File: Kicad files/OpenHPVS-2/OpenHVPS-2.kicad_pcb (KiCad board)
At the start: 2 copper layers, 45.8 x 20.5 mm, 69 parts, among them J1 Conn_01x03_Male, J2 Conn_01x03_Male, Q1 FQT7N10, Q2 BC846A, Q3 MMDT3906, U1 MAX6008AEUR+T, U2 74HC14, U3 MAX4162, U4 CD14538BM

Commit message: Forgot the supply to the opamp - added. changed a capacitor value
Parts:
- C1: value 0.1uF -> 150pF
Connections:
- C2 pad 1: Net-(C2-Pad1) -> Net-(U3-Pad5)
- R5 pad 1: Net-(C2-Pad1) -> Net-(U3-Pad5)
- U2 pad 14: Net-(C2-Pad1) -> Net-(U3-Pad5)
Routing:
- net Net-(U3-Pad5): track 0.00 -> 8.95 mm
- net Net-(C2-Pad1): track 8.95 -> 0.00 mm

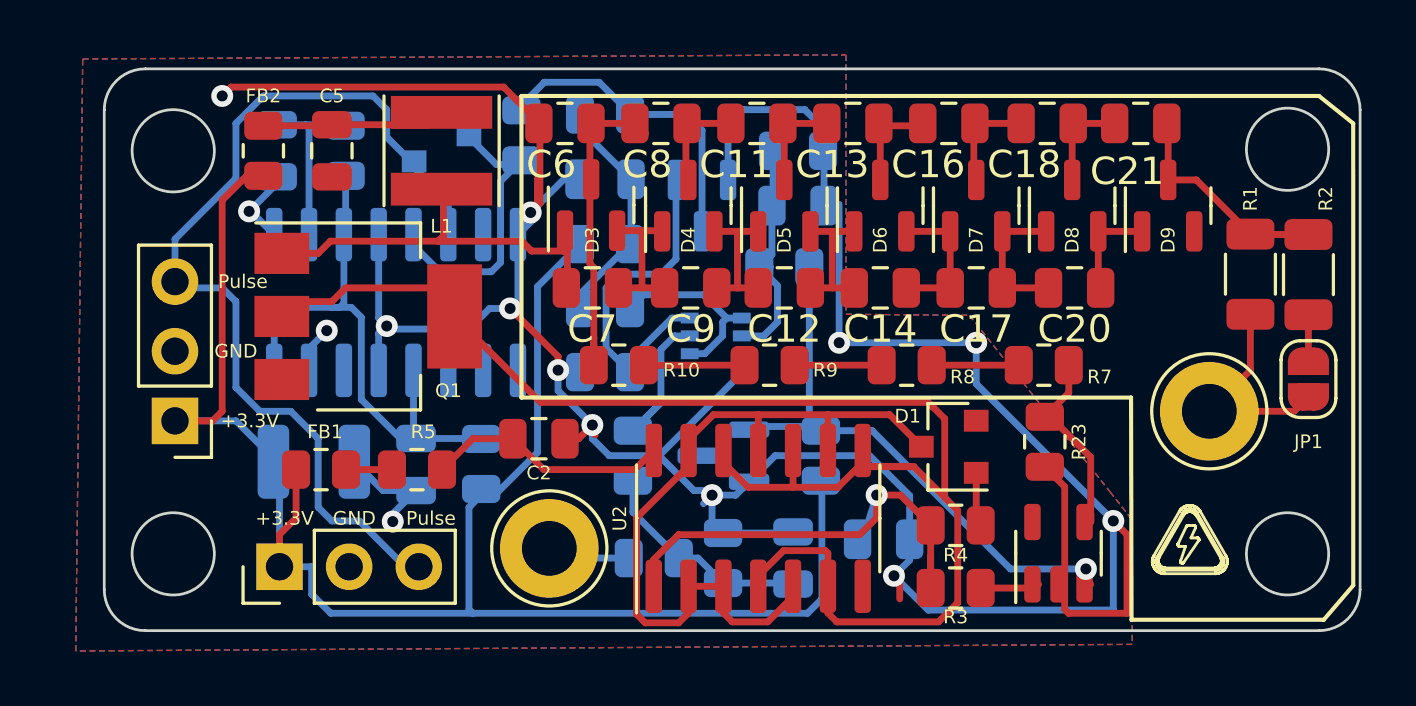
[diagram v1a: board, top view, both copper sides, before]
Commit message: Added space at  bottom and routed  track +graphic.
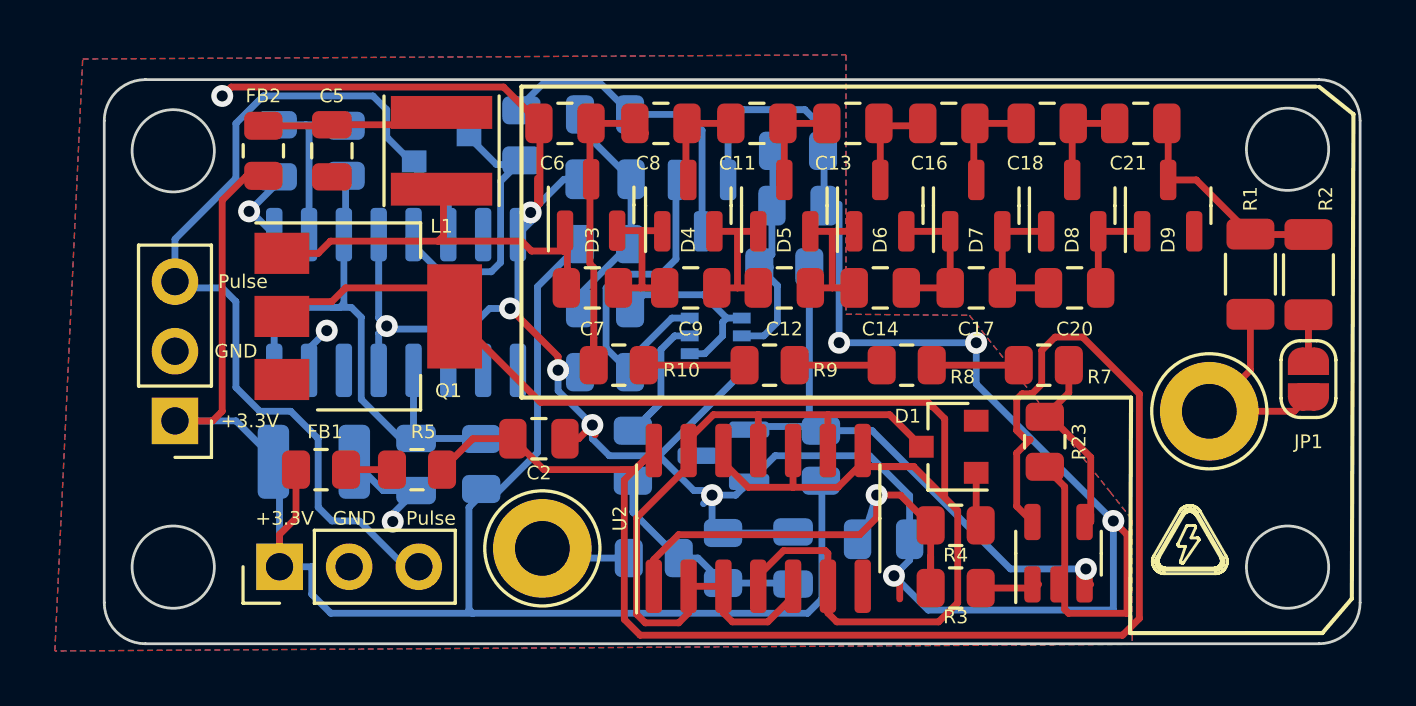
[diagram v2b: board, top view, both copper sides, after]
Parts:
- moved H1 0.25 mm to (138.2, 74.5)
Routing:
- net Net-(U3-Pad5): track 8.95 -> 55.2 mm
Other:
- board size 45.8 x 20.5 mm -> 45.8 x 20.6 mm

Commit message: Fixed trace too close to Anode. flipped U3 to other side
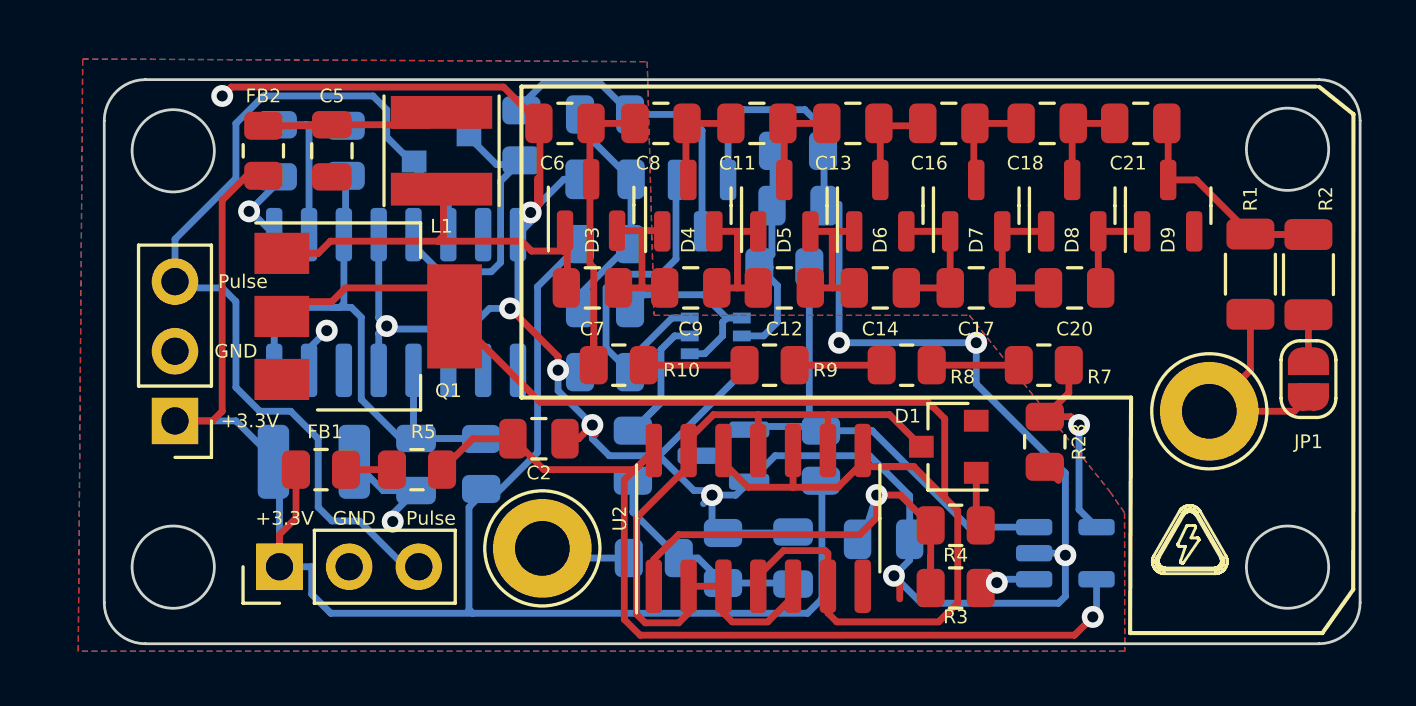
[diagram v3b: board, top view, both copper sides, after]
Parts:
- U3: moved to B.Cu
- moved U3 0.25 mm to (157.2, 74.7), turned to 0 degrees
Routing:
- net Net-(U3-Pad5): track 55.2 -> 34.6 mm, vias 0 -> 1
- net GND: track 131.4 -> 118.9 mm
- net +2V5: track 21.3 -> 18.1 mm, vias 1 -> 0
- net Net-(R23-Pad1): track 7.43 -> 8.04 mm, vias 0 -> 1
- net Net-(R3-Pad2): track 2.17 -> 2.08 mm, vias 0 -> 1
